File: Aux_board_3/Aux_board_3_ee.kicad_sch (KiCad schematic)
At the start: 21 parts, among them J2 P04d, J3 MODBUS, Q33 BSS138KJ, Q34 BSS138KJ, Q35 BSS138KJ, U3 SN75LBC179AD

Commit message: finished Board 3 schematic
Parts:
- renumbered R97 to R10, R98 to R11, R99 to R12, R92 to R5, R93 to R6, R94 to R7, R95 to R8, R96 to R9
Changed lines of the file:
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@@
 	(title_block
 		(title "Karcsi (INDACT Robot Arm) - Aux. Control Board 3")
-		(date "2024-05-04")
+		(date "2024-05-09")
 		(rev "1.0")
 		(company "LEGO Kör (legokor.hu)")
@@
 		(dnp no)
 		(fields_autoplaced yes)
-		(property "Reference" "R95"
+		(property "Reference" "R8"
 			(at 91.44 105.4099 0)
 			(effects
@@
 			(project "Aux_board_3"
 				(path "/aaa7ce82-fd86-4c66-99d9-b7746a947d4d/8706d3f3-5555-4f61-80b0-4a68e9b28181"
-					(reference "R95")
+					(reference "R8")
 					(unit 1)
 				)
@@
 		(dnp no)
 		(fields_autoplaced yes)
-		(property "Reference" "R97"
+		(property "Reference" "R10"
 			(at 140.97 105.4099 0)
 			(effects
@@
 			(project "Aux_board_3"
 				(path "/aaa7ce82-fd86-4c66-99d9-b7746a947d4d/8706d3f3-5555-4f61-80b0-4a68e9b28181"
-					(reference "R97")
+					(reference "R10")
 					(unit 1)
 				)
@@
 		(on_board yes)
 		(dnp no)
-		(fields_autoplaced yes)
-		(property "Reference" "R93"
+		(property "Reference" "R6"
 			(at 182.88 44.45 0)
 			(effects
@@
 			(project "Aux_board_3"
 				(path "/aaa7ce82-fd86-4c66-99d9-b7746a947d4d/8706d3f3-5555-4f61-80b0-4a68e9b28181"
-					(reference "R93")
+					(reference "R6")
 					(unit 1)
 				)
@@
 		(dnp no)
 		(fields_autoplaced yes)
-		(property "Reference" "R99"
+		(property "Reference" "R12"
 			(at 191.77 105.4099 0)
 			(effects
@@
 			(project "Aux_board_3"
 				(path "/aaa7ce82-fd86-4c66-99d9-b7746a947d4d/8706d3f3-5555-4f61-80b0-4a68e9b28181"
-					(reference "R99")
+					(reference "R12")
 					(unit 1)
 				)
@@
 		(dnp no)
 		(fields_autoplaced yes)
-		(property "Reference" "R96"
+		(property "Reference" "R9"
 			(at 132.08 126.9999 0)
 			(effects
@@
 			(project "Aux_board_3"
 				(path "/aaa7ce82-fd86-4c66-99d9-b7746a947d4d/8706d3f3-5555-4f61-80b0-4a68e9b28181"
-					(reference "R96")
+					(reference "R9")
 					(unit 1)
 				)
@@
 		(on_board yes)
 		(dnp no)
-		(property "Reference" "R92"
+		(property "Reference" "R5"
 			(at 141.605 40.64 0)
 			(effects
@@
 			(project "Aux_board_3"
 				(path "/aaa7ce82-fd86-4c66-99d9-b7746a947d4d/8706d3f3-5555-4f61-80b0-4a68e9b28181"
-					(reference "R92")
+					(reference "R5")
 					(unit 1)
 				)
@@
 		(dnp no)
 		(fields_autoplaced yes)
-		(property "Reference" "R98"
+		(property "Reference" "R11"
 			(at 182.88 126.9999 0)
 			(effects
@@
 			(project "Aux_board_3"
 				(path "/aaa7ce82-fd86-4c66-99d9-b7746a947d4d/8706d3f3-5555-4f61-80b0-4a68e9b28181"
-					(reference "R98")
+					(reference "R11")
 					(unit 1)
 				)
@@
 		(dnp no)
 		(fields_autoplaced yes)
-		(property "Reference" "R94"
+		(property "Reference" "R7"
 			(at 82.55 126.9999 0)
 			(effects
@@
 			(project "Aux_board_3"
 				(path "/aaa7ce82-fd86-4c66-99d9-b7746a947d4d/8706d3f3-5555-4f61-80b0-4a68e9b28181"
-					(reference "R94")
+					(reference "R7")
 					(unit 1)
 				)

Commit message: Board 3 layout started
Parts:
- J3: footprint (none) -> Connector_PinHeader_1.00mm:PinHeader_1x04_P1.00mm_Horizontal; Supplier (none) -> LEGOlab; Supplier item no (none) -> -
- U3: MF (none) -> Texas Instruments; Package SOIC-8 Texas Instruments -> (none)

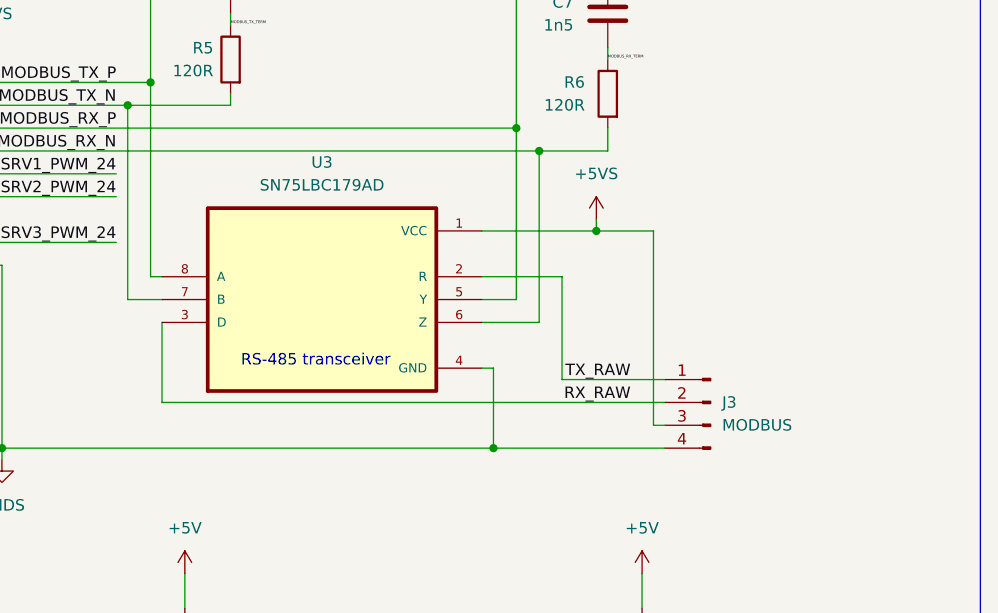
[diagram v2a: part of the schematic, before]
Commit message: Board 3 MODBUS and servos done
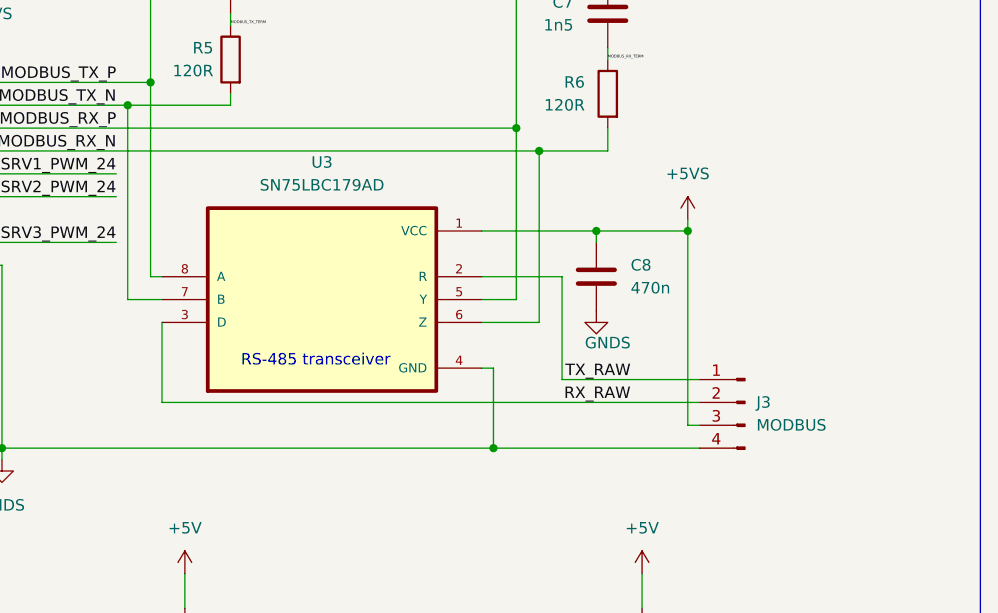
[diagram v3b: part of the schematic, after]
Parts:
- added C8: 470n, Capacitor_SMD:C_0805_2012Metric_Pad1.18x1.45mm_HandSolder, symbol Device:C
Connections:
- net +5VS: now also C8.1
- net GNDS: now also C8.2
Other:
- moved on the sheet: J3
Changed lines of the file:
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@@
 	)
 	(junction
+		(at 194.31 60.96)
+		(diameter 0)
+		(color 0 0 0 0)
+	)
+	(junction
 		(at 83.82 49.53)
 		(diameter 0)
@@
 	(wire
 		(pts
-			(xy 184.15 60.96) (xy 190.5 60.96)
+			(xy 88.9 59.69) (xy 88.9 62.23)
 		)
 		(stroke
@@
 	(wire
 		(pts
-			(xy 88.9 59.69) (xy 88.9 62.23)
+			(xy 138.43 124.46) (xy 138.43 133.35)
 		)
 		(stroke
@@
 	(wire
 		(pts
-			(xy 138.43 124.46) (xy 138.43 133.35)
+			(xy 115.57 49.53) (xy 175.26 49.53)
 		)
 		(stroke
@@
 	(wire
 		(pts
-			(xy 115.57 49.53) (xy 175.26 49.53)
+			(xy 132.08 46.99) (xy 132.08 68.58)
 		)
 		(stroke
@@
 	(wire
 		(pts
-			(xy 132.08 46.99) (xy 132.08 68.58)
+			(xy 194.31 60.96) (xy 184.15 60.96)
 		)
 		(stroke
@@
 	(wire
 		(pts
-			(xy 180.34 77.47) (xy 191.77 77.47)
+			(xy 180.34 77.47) (xy 195.58 77.47)
 		)
 		(stroke
@@
 	(wire
 		(pts
-			(xy 190.5 82.55) (xy 191.77 82.55)
+			(xy 194.31 82.55) (xy 195.58 82.55)
 		)
 		(stroke
@@
 	(wire
 		(pts
-			(xy 184.15 59.69) (xy 184.15 60.96)
+			(xy 194.31 59.69) (xy 194.31 60.96)
 		)
 		(stroke
@@
 	(wire
 		(pts
-			(xy 190.5 60.96) (xy 190.5 82.55)
+			(xy 194.31 60.96) (xy 194.31 82.55)
 		)
 		(stroke
@@
 	(wire
 		(pts
+			(xy 184.15 62.23) (xy 184.15 60.96)
+		)
+		(stroke
+			(width 0)
+			(type default)
+		)
+	)
+	(wire
+		(pts
 			(xy 77.47 46.99) (xy 77.47 49.53)
 		)
@@
 	(wire
 		(pts
-			(xy 191.77 85.09) (xy 172.72 85.09)
+			(xy 195.58 85.09) (xy 172.72 85.09)
 		)
 		(stroke
@@
 	(wire
 		(pts
-			(xy 135.89 80.01) (xy 191.77 80.01)
+			(xy 135.89 80.01) (xy 195.58 80.01)
 		)
 		(stroke
@@
 	(symbol
 		(lib_id "power:+5V")
-		(at 184.15 59.69 0)
+		(at 194.31 59.69 0)
 		(unit 1)
 		(exclude_from_sim no)
@@
 		(fields_autoplaced yes)
 		(property "Reference" "#PWR081"
-			(at 184.15 63.5 0)
+			(at 194.31 63.5 0)
 			(effects
 				(font
@@
 		)
 		(property "Value" "+5VS"
-			(at 184.15 54.61 0)
+			(at 194.31 54.61 0)
 			(effects
 				(font
@@
 		)
 		(property "Footprint" ""
-			(at 184.15 59.69 0)
+			(at 194.31 59.69 0)
 			(effects
 				(font
@@
 		)
 		(property "Datasheet" ""
-			(at 184.15 59.69 0)
+			(at 194.31 59.69 0)
 			(effects
 				(font
@@
 		)
 		(property "Description" "Power symbol creates a global label with name \"+5V\""
-			(at 184.15 59.69 0)
+			(at 194.31 59.69 0)
 			(effects
 				(font
@@
 	(symbol
 		(lib_id "Device:C")
+		(at 184.15 66.04 0)
+		(unit 1)
+		(exclude_from_sim no)
+		(in_bom yes)
+		(on_board yes)
+		(dnp no)
+		(fields_autoplaced yes)
+		(property "Reference" "C8"
+			(at 187.96 64.7699 0)
+			(effects
+				(font
+					(size 1.27 1.27)
+				)
+				(justify left)
+			)
+		)
+		(property "Value" "470n"
+			(at 187.96 67.3099 0)
+			(effects
+				(font
+					(size 1.27 1.27)
+				)
+				(justify left)
+			)
+		)
+		(property "Footprint" "Capacitor_SMD:C_0805_2012Metric_Pad1.18x1.45mm_HandSolder"
+			(at 185.1152 69.85 0)
+			(effects
+				(font
+					(size 1.27 1.27)
+				)
+				(hide yes)
+			)
+		)
+		(property "Datasheet" "~"
+			(at 184.15 66.04 0)
+			(effects
+				(font
+					(size 1.27 1.27)
+				)
+				(hide yes)
+			)
+		)
+		(property "Description" "Unpolarized capacitor"
+			(at 184.15 66.04 0)
+			(effects
+				(font
+					(size 1.27 1.27)
+				)
+				(hide yes)
+			)
+		)
+		(property "Sourced" "1"
+			(at 184.15 66.04 0)
+			(effects
+				(font
+					(size 1.27 1.27)
+				)
+				(hide yes)
+			)
+		)
+		(property "Supplier" "Lomex"
+			(at 184.15 66.04 0)
+			(effects
+				(font
+					(size 1.27 1.27)
+				)
+				(hide yes)
+			)
+		)
+		(property "Supplier item no" "82-14-68"
+			(at 184.15 66.04 0)
+			(effects
+				(font
+					(size 1.27 1.27)
+				)
+				(hide yes)
+			)
+		)
+		(pin "2"
+		)
+		(pin "1"
+		)
+		(instances
+			(project "Aux_board_3"
+				(path "/aaa7ce82-fd86-4c66-99d9-b7746a947d4d/8706d3f3-5555-4f61-80b0-4a68e9b28181"
+					(reference "C8")
+					(unit 1)
+				)
+			)
+		)
+	)
+	(symbol
+		(lib_id "Device:C")
 		(at 143.51 33.02 0)
 		(mirror y)
@@
 	(symbol
 		(lib_id "power:GNDS")
+		(at 184.15 69.85 0)
+		(unit 1)
+		(exclude_from_sim no)
+		(in_bom yes)
+		(on_board yes)
+		(dnp no)
+		(property "Reference" "#PWR041"
+			(at 184.15 76.2 0)
+			(effects
+				(font
+					(size 1.27 1.27)
+				)
+				(hide yes)
+			)
+		)
+		(property "Value" "GNDS"
+			(at 185.42 73.406 0)
+			(effects
+				(font
+					(size 1.27 1.27)
+				)
+			)
+		)
+		(property "Footprint" ""
+			(at 184.15 69.85 0)
+			(effects
+				(font
+					(size 1.27 1.27)
+				)
+				(hide yes)
+			)
+		)
+		(property "Datasheet" ""
+			(at 184.15 69.85 0)
+			(effects
+				(font
+					(size 1.27 1.27)
+				)
+				(hide yes)
+			)
+		)
+		(property "Description" "Power symbol creates a global label with name \"GNDS\" , signal ground"
+			(at 184.15 69.85 0)
+			(effects
+				(font
+					(size 1.27 1.27)
+				)
+				(hide yes)
+			)
+		)
+		(pin "1"
+		)
+		(instances
+			(project "Aux_board_3"
+				(path "/aaa7ce82-fd86-4c66-99d9-b7746a947d4d/8706d3f3-5555-4f61-80b0-4a68e9b28181"
+					(reference "#PWR041")
+					(unit 1)
+				)
+			)
+		)
+	)
+	(symbol
+		(lib_id "power:GNDS")
 		(at 118.11 86.36 0)
 		(unit 1)
@@
 	(symbol
 		(lib_id "Connector:Conn_01x04_Pin")
-		(at 196.85 80.01 0)
+		(at 200.66 80.01 0)
 		(mirror y)
 		(unit 1)
@@
 		(fields_autoplaced yes)
 		(property "Reference" "J3"
-			(at 198.12 80.0099 0)
+			(at 201.93 80.0099 0)
 			(effects
 				(font
@@
 		)
 		(property "Value" "MODBUS"
-			(at 198.12 82.5499 0)
+			(at 201.93 82.5499 0)
 			(effects
 				(font
@@
 		)
 		(property "Footprint" "Connector_PinHeader_1.00mm:PinHeader_1x04_P1.00mm_Horizontal"
-			(at 196.85 80.01 0)
+			(at 200.66 80.01 0)
 			(effects
 				(font
@@
 		)
 		(property "Datasheet" "~"
-			(at 196.85 80.01 0)
+			(at 200.66 80.01 0)
 			(effects
 				(font
@@
 		)
 		(property "Description" "Generic connector, single row, 01x04, script generated"
-			(at 196.85 80.01 0)
+			(at 200.66 80.01 0)
 			(effects
 				(font
@@
 		)
 		(property "Supplier" "LEGOlab"
-			(at 196.85 80.01 0)
+			(at 200.66 80.01 0)
 			(effects
 				(font
@@
 		)
 		(property "Supplier item no" "-"
-			(at 196.85 80.01 0)
+			(at 200.66 80.01 0)
 			(effects
 				(font
@@
 		)
 		(property "Package" ""
-			(at 196.85 80.01 0)
+			(at 200.66 80.01 0)
 			(effects
 				(font
